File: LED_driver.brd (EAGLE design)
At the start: 38.6 x 25.4 mm, 16 parts

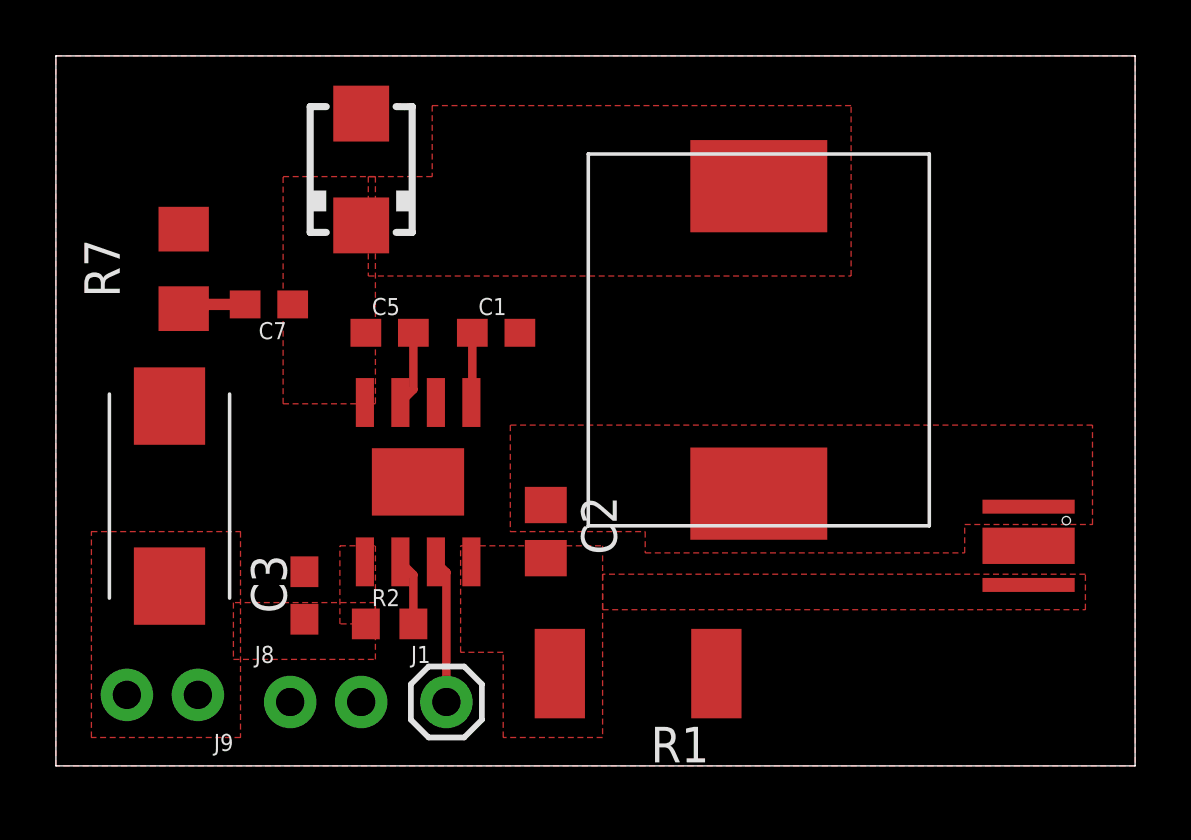
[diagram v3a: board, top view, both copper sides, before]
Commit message: Made several improvements and allowed for the LED to be wired with through holes
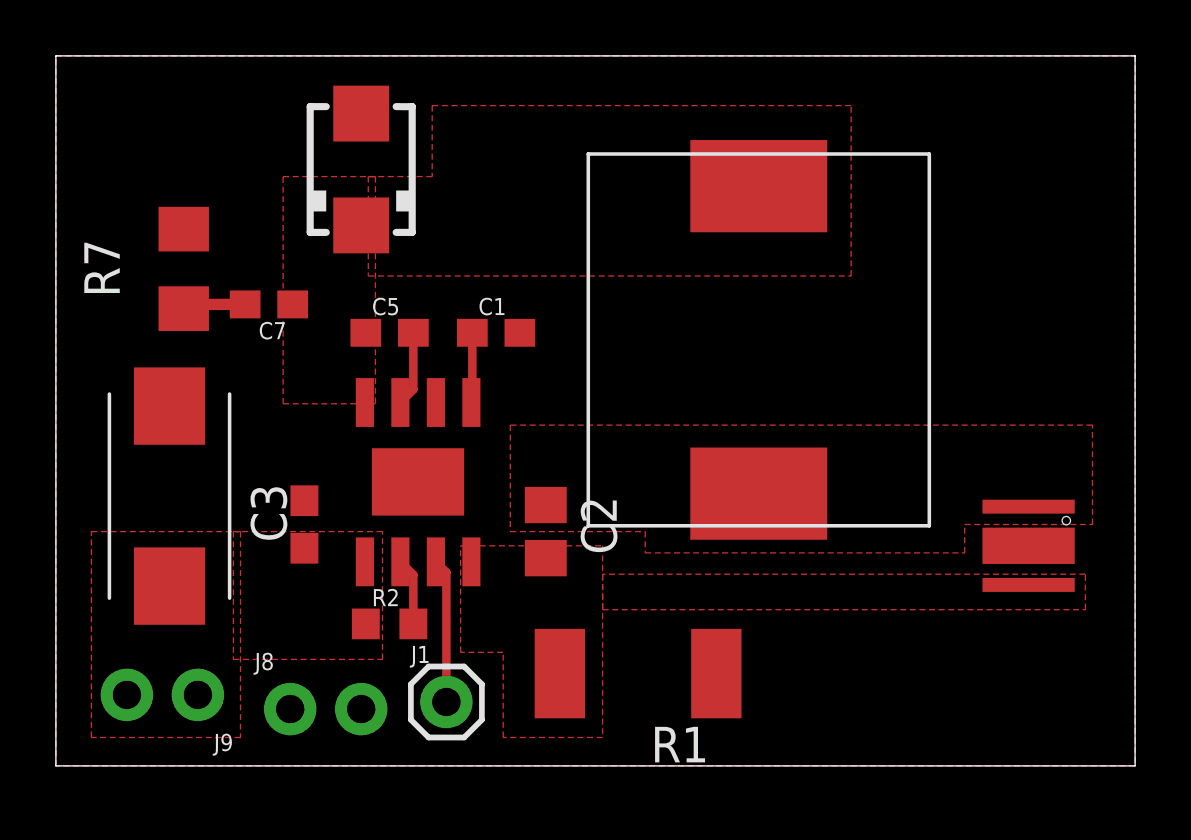
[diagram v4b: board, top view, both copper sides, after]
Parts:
- moved C3 2.54 mm to (8.89, 8.64)
- moved J8 0.25 mm to (8.38, 2.03)
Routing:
- added copper zone on layer 16, net GND
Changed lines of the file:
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@@
 <element name="C8" library="PowerComponents" package="CTAN(7.30_4.30MM)" value="47uF" x="4.064" y="9.652" smashed="yes" rot="R90"/>
 <element name="J1" library="SparkFun-Connectors" library_urn="urn:adsk.eagle:library:513" package="1X01" package3d_urn="urn:adsk.eagle:package:38028/1" value="" x="13.97" y="2.286"/>
-<element name="C3" library="rcl" library_urn="urn:adsk.eagle:library:334" package="C0603" package3d_urn="urn:adsk.eagle:package:23616/2" value="4.7uF" x="8.89" y="6.096" smashed="yes" rot="R90">
-<attribute name="NAME" x="8.255" y="5.461" size="1.27" layer="25" rot="R90"/>
+<element name="C3" library="rcl" library_urn="urn:adsk.eagle:library:334" package="C0603" package3d_urn="urn:adsk.eagle:package:23616/2" value="4.7uF" x="8.89" y="8.636" smashed="yes" rot="R90">
+<attribute name="NAME" x="8.255" y="8.001" size="1.27" layer="25" rot="R90"/>
 </element>
-<element name="J8" library="SparkFun-Connectors" library_urn="urn:adsk.eagle:library:513" package="1X02_NO_SILK" package3d_urn="urn:adsk.eagle:package:38051/1" value="" x="8.382" y="2.286"/>
+<element name="J8" library="SparkFun-Connectors" library_urn="urn:adsk.eagle:library:513" package="1X02_NO_SILK" package3d_urn="urn:adsk.eagle:package:38051/1" value="" x="8.382" y="2.032"/>
 <element name="J9" library="SparkFun-Connectors" library_urn="urn:adsk.eagle:library:513" package="1X02_NO_SILK" package3d_urn="urn:adsk.eagle:package:38051/1" value="" x="5.08" y="2.54" rot="R180"/>
 <element name="U$3" library="LED_00H53" package="LED_00H53" value="LED_00H53" x="34.798" y="7.874" rot="R270"/>
@@
 <vertex x="38.608" y="25.4"/>
 <vertex x="38.608" y="0"/>
+</polygon>
+<polygon width="0.1524" layer="16">
+<vertex x="0" y="25.4"/>
+<vertex x="38.608" y="25.4"/>
+<vertex x="38.608" y="0"/>
+<vertex x="0" y="0"/>
 </polygon>
 </signal>
@@
 <polygon width="0.1524" layer="1">
 <vertex x="6.35" y="3.81"/>
-<vertex x="11.43" y="3.81"/>
-<vertex x="11.43" y="5.842"/>
-<vertex x="6.35" y="5.842"/>
-</polygon>
-<polygon width="0.1524" layer="1">
-<vertex x="11.43" y="5.08"/>
-<vertex x="10.16" y="5.08"/>
-<vertex x="10.16" y="7.874"/>
-<vertex x="11.43" y="7.874"/>
+<vertex x="11.684" y="3.81"/>
+<vertex x="11.684" y="8.382"/>
+<vertex x="6.35" y="8.382"/>
 </polygon>
 </signal>
